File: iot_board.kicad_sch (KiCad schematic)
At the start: 4 parts, among them J1 SS-52400-003, J2 B2B-PH-SM4-TB, U2 MCP73871-2CAI_ML

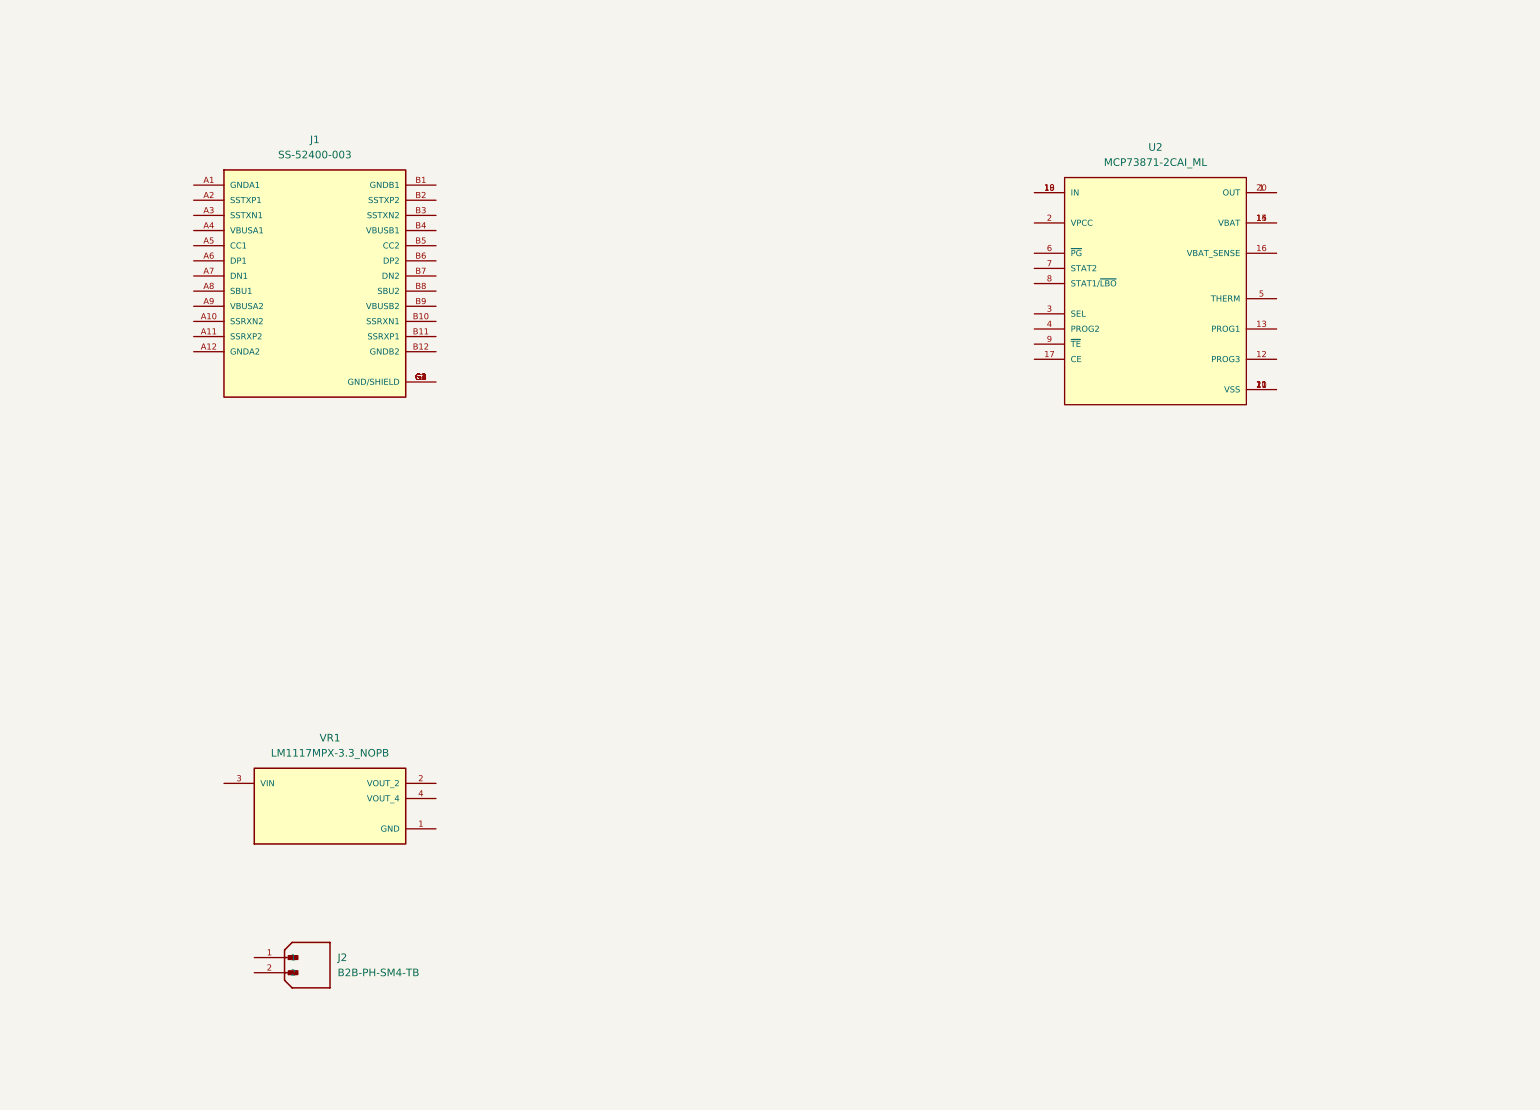
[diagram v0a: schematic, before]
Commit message: Connected the USB-C connector and the Li-Polymer battery charger
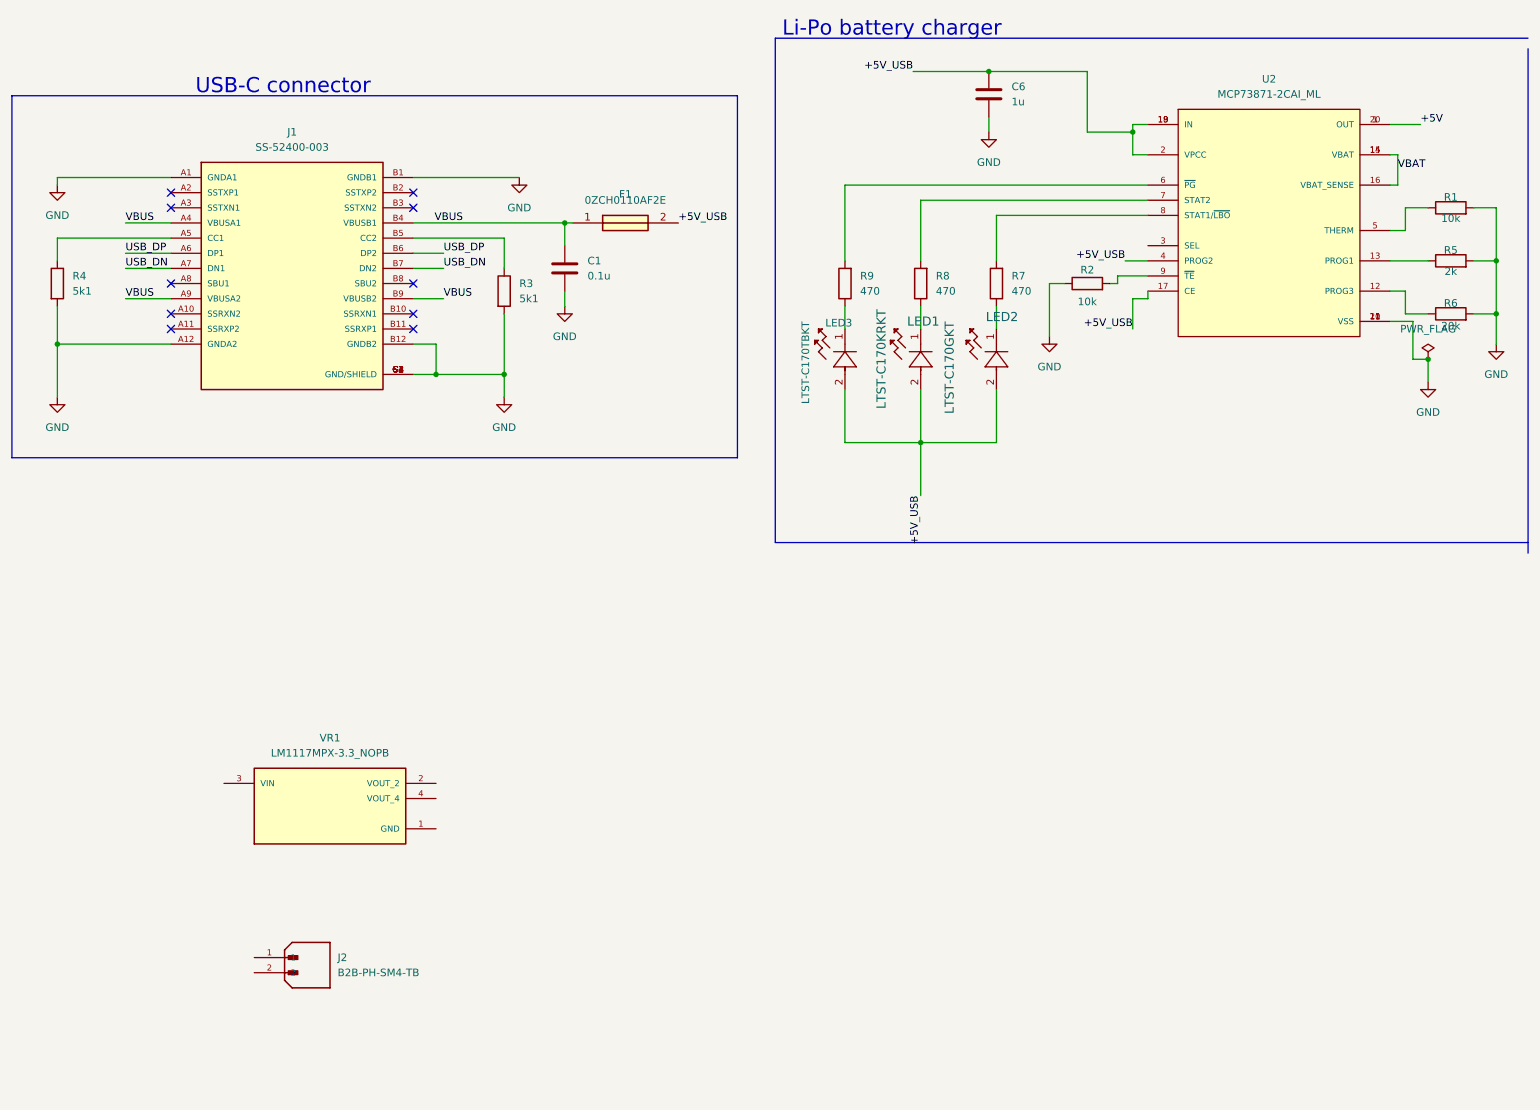
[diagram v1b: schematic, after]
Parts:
- added C1: 0.1u, symbol Device:C
- added C6: 1u, symbol Device:C
- added F1: 0ZCH0110AF2E, symbol ESP32_IoT_Board_Schem:0ZCH0110AF2E
- added LED1: LTST-C170KRKT, ESP32_IoT_Board_Footprint:LTST-C170KRKT, symbol ESP32_IoT_Board_Schem:LTST-C170KRKT
- added LED2: LTST-C170GKT, symbol ESP32_IoT_Board_Schem:LTST-C170GKT
- added LED3: LTST-C170TBKT, ESP32_IoT_Board_Footprint:LTST-C170TBKT, symbol ESP32_IoT_Board_Schem:LTST-C170TBKT
- added R1, R2: 10k, symbol Device:R
- added R3, R4: 5k1, symbol Device:R
- added R5: 2k, symbol Device:R
- added R6: 20k, symbol Device:R
- added R7, R8, R9: 470, symbol Device:R
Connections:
- net +5V: now reaches U2.1 (OUT), U2.20 (OUT)
- net GND: now reaches U2.10 (VSS), U2.11 (VSS), U2.21 (VSS)
- net GND: now also J1.A1 (GNDA1), J1.A12 (GNDA2), J1.B1 (GNDB1), J1.B12 (GNDB2), J1.G1 (GND/SHIELD), J1.G2 (GND/SHIELD), J1.G3 (GND/SHIELD), J1.G4 (GND/SHIELD), J1.S1 (GND/SHIELD), J1.S2 (GND/SHIELD), J1.S3 (GND/SHIELD), J1.S4 (GND/SHIELD), C1.2, C6.2, R1.2, R2.1, R3.2, R4.2, R5.2, R6.2
- net at U2.12 (PROG3): now also R6.1
- net at U2.13 (PROG1): now also R5.1
- net VBAT: now reaches U2.14 (VBAT), U2.15 (VBAT)
- net VBAT: now also U2.16 (VBAT_SENSE)
- net +5V_USB: now reaches U2.17 (CE)
- net +5V_USB: now also U2.18 (IN), U2.19 (IN), U2.2 (VPCC), U2.4 (PROG2), C6.1, F1.2, LED1.2, LED2.2, LED3.2
- net at U2.5 (THERM): now also R1.1
- net at U2.6 (~{PG}): now also R9.2
- net at U2.7 (STAT2): now also R8.2
- net at U2.8 (STAT1/~{LBO}): now also R7.2
- net at U2.9 (~{TE}): now also R2.2
- net VBUS: now reaches J1.A4 (VBUSA1)
- net VBUS: now also J1.A9 (VBUSA2), J1.B4 (VBUSB1), J1.B9 (VBUSB2), C1.1, F1.1
- net at J1.A5 (CC1): now also R4.1
- net USB_DP: now reaches J1.A6 (DP1)
- net USB_DP: now also J1.B6 (DP2)
- net USB_DN: now reaches J1.A7 (DN1)
- net USB_DN: now also J1.B7 (DN2)
- net at J1.B5 (CC2): now also R3.1
- new net: LED1.1, R8.1
- new net: LED3.1, R9.1
- new net: LED2.1, R7.1
- no-connect marks 0 -> 10
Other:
- note added: "Li-Po battery charger"
- note added: "USB-C connector"
- moved on the sheet: J1, U2

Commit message: Added ESP32 microcontroller and SMD card connector
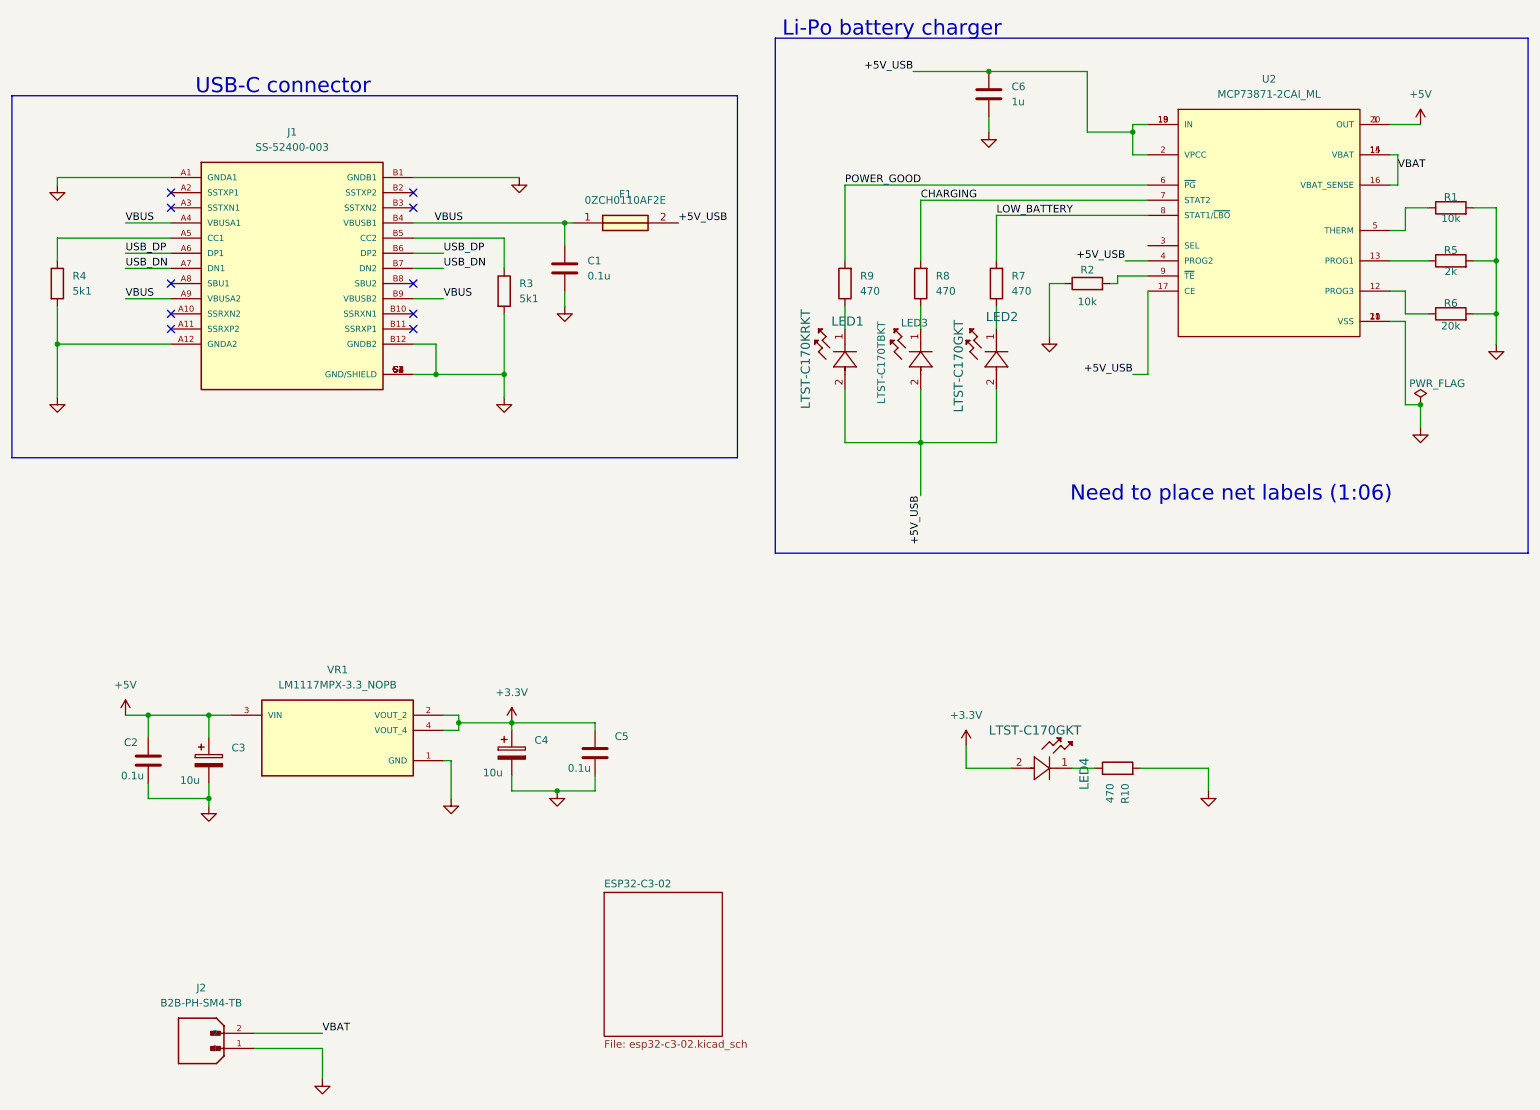
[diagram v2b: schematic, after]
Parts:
- added C2, C5: 0.1u, symbol Device:C
- added C3, C4: 10u, symbol Device:C_Polarized
- added LED4: LTST-C170GKT, symbol ESP32_IoT_Board_Schem:LTST-C170GKT
- added R10: 470, symbol Device:R
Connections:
- net +5V: now also VR1.3 (VIN), C2.1, C3.1
- net GND: now also J2.1, VR1.1 (GND), C2.2, C3.2, C4.2, C5.2, R10.2
- net VBAT: now also J2.2
- net +3.3V: now reaches VR1.2 (VOUT_2)
- net +3.3V: now also VR1.4 (VOUT_4), C4.1, C5.1, LED4.2
- net at R8.1: now also LED3.1; no longer LED1.1
- net CHARGING: now reaches R8.2, U2.7 (STAT2)
- net at R9.1: now also LED1.1; no longer LED3.1
- net POWER_GOOD: now reaches R9.2, U2.6 (~{PG})
- net LOW_BATTERY: now reaches R7.2, U2.8 (STAT1/~{LBO})
- new net: LED4.1, R10.1
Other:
- added sheet ESP32-C3-02 (esp32-c3-02.kicad_sch)
- note added: "Need to place net labels (1:06)"
- moved on the sheet: J2, LED1, LED3, VR1

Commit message: Connected USB to UART connector, ESP32 controller and the SD card module
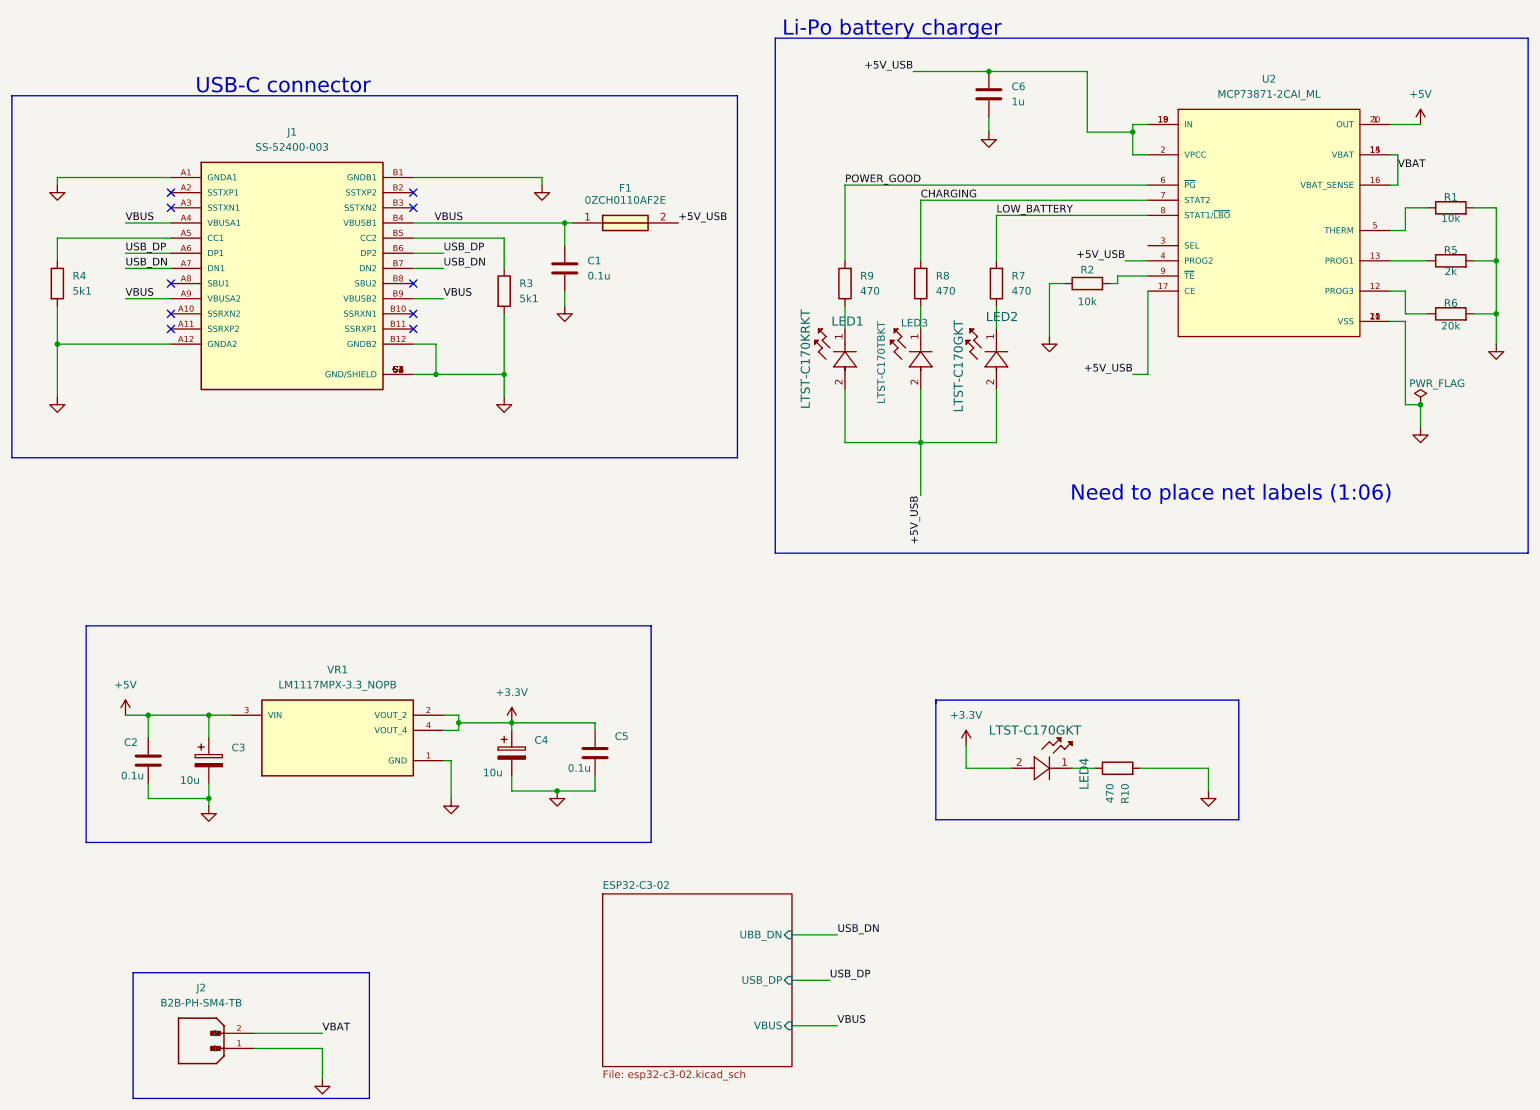
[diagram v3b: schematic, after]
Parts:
- F1: footprint (none) -> ESP32_IoT_Board_Footprint:0ZCH0110AF2E
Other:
- sheet ESP32-C3-02 ports: added UBB_DN, USB_DP, VBUS; removed none
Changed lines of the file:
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@@
 	(wire
 		(pts
+			(xy 146.05 166.37) (xy 153.67 166.37)
+		)
+		(stroke
+			(width 0)
+			(type default)
+		)
+	)
+	(wire
+		(pts
 			(xy 34.29 129.54) (xy 38.1 129.54)
 		)
@@
 		)
 	)
+	(polyline
+		(pts
+			(xy 170.18 147.066) (xy 220.98 147.066)
+		)
+		(stroke
+			(width 0)
+			(type default)
+		)
+	)
 	(wire
 		(pts
@@
 		)
 	)
+	(polyline
+		(pts
+			(xy 122.428 150.876) (xy 122.428 114.554)
+		)
+		(stroke
+			(width 0)
+			(type default)
+		)
+	)
 	(wire
 		(pts
@@
 	(polyline
 		(pts
+			(xy 27.686 114.554) (xy 122.428 114.554)
+		)
+		(stroke
+			(width 0)
+			(type default)
+		)
+	)
+	(polyline
+		(pts
+			(xy 35.56 172.72) (xy 75.184 172.72)
+		)
+		(stroke
+			(width 0)
+			(type default)
+		)
+	)
+	(polyline
+		(pts
 			(xy 136.906 25.654) (xy 136.906 86.36)
 		)
@@
 		)
 	)
+	(polyline
+		(pts
+			(xy 75.184 193.802) (xy 75.184 172.72)
+		)
+		(stroke
+			(width 0)
+			(type default)
+		)
+	)
+	(polyline
+		(pts
+			(xy 35.56 172.72) (xy 35.56 193.802)
+		)
+		(stroke
+			(width 0)
+			(type default)
+		)
+	)
+	(polyline
+		(pts
+			(xy 27.686 150.876) (xy 122.428 150.876)
+		)
+		(stroke
+			(width 0)
+			(type default)
+		)
+	)
 	(wire
 		(pts
@@
 		)
 	)
+	(polyline
+		(pts
+			(xy 170.18 127) (xy 170.18 127.508)
+		)
+		(stroke
+			(width 0)
+			(type default)
+		)
+	)
 	(wire
 		(pts
@@
 		)
 	)
+	(polyline
+		(pts
+			(xy 27.686 114.554) (xy 27.686 150.876)
+		)
+		(stroke
+			(width 0)
+			(type default)
+		)
+	)
 	(wire
 		(pts
@@
 		)
 	)
+	(polyline
+		(pts
+			(xy 220.98 127) (xy 170.18 127)
+		)
+		(stroke
+			(width 0)
+			(type default)
+		)
+	)
 	(wire
 		(pts
@@
 	(wire
 		(pts
+			(xy 146.05 173.99) (xy 152.4 173.99)
+		)
+		(stroke
+			(width 0)
+			(type default)
+		)
+	)
+	(wire
+		(pts
 			(xy 34.29 52.07) (xy 41.91 52.07)
 		)
@@
 		)
 	)
+	(polyline
+		(pts
+			(xy 220.98 147.066) (xy 220.98 127)
+		)
+		(stroke
+			(width 0)
+			(type default)
+		)
+	)
 	(wire
 		(pts
@@
 	(wire
 		(pts
-			(xy 246.38 58.42) (xy 248.92 58.42)
+			(xy 104.14 40.64) (xy 104.14 39.37)
 		)
 		(stroke
@@
 	(wire
 		(pts
-			(xy 82.55 39.37) (xy 100.33 39.37)
+			(xy 104.14 39.37) (xy 82.55 39.37)
+		)
+		(stroke
+			(width 0)
+			(type default)
+		)
+	)
+	(wire
+		(pts
+			(xy 246.38 58.42) (xy 248.92 58.42)
 		)
 		(stroke
@@
 		)
 	)
+	(polyline
+		(pts
+			(xy 35.56 193.802) (xy 75.184 193.802)
+		)
+		(stroke
+			(width 0)
+			(type default)
+		)
+	)
 	(wire
 		(pts
@@
 		)
 	)
+	(polyline
+		(pts
+			(xy 170.18 127) (xy 170.18 147.066)
+		)
+		(stroke
+			(width 0)
+			(type default)
+		)
+	)
 	(wire
 		(pts
@@
 		)
 	)
+	(wire
+		(pts
+			(xy 146.05 181.61) (xy 153.67 181.61)
+		)
+		(stroke
+			(width 0)
+			(type default)
+		)
+	)
 	(label "CHARGING"
 		(at 167.64 43.18 0)
@@
 		)
 	)
+	(label "USB_DN"
+		(at 153.67 166.37 0)
+		(effects
+			(font
+				(size 1.27 1.27)
+			)
+			(justify left bottom)
+		)
+	)
+	(label "VBUS"
+		(at 153.67 181.61 0)
+		(effects
+			(font
+				(size 1.27 1.27)
+			)
+			(justify left bottom)
+		)
+	)
+	(label "USB_DP"
+		(at 152.4 173.99 0)
+		(effects
+			(font
+				(size 1.27 1.27)
+			)
+			(justify left bottom)
+		)
+	)
 	(symbol
 		(lib_id "power:+3.3V")
@@
 		(dnp no)
 		(property "Reference" "F1"
-			(at 118.11 42.164 0)
+			(at 118.11 41.148 0)
 			(effects
 				(font
@@
 			)
 		)
-		(property "Footprint" ""
+		(property "Footprint" "ESP32_IoT_Board_Footprint:0ZCH0110AF2E"
 			(at 132.08 143.18 0)
 			(effects
@@
 	(symbol
 		(lib_id "power:GND")
-		(at 100.33 39.37 0)
+		(at 104.14 40.64 0)
 		(unit 1)
 		(exclude_from_sim no)
@@
 		(dnp no)
 		(property "Reference" "#PWR06"
-			(at 100.33 45.72 0)
+			(at 104.14 46.99 0)
 			(effects
 				(font
@@
 		)
 		(property "Value" "GND"
-			(at 100.33 44.45 0)
+			(at 104.14 45.72 0)
 			(effects
 				(font
@@
 		)
 		(property "Footprint" ""
-			(at 100.33 39.37 0)
+			(at 104.14 40.64 0)
 			(effects
 				(font
@@
 		)
 		(property "Datasheet" ""
-			(at 100.33 39.37 0)
+			(at 104.14 40.64 0)
 			(effects
 				(font
@@
 		)
 		(property "Description" "Power symbol creates a global label with name \"GND\" , ground"
-			(at 100.33 39.37 0)
+			(at 104.14 40.64 0)
 			(effects
 				(font
@@
 	)
 	(sheet
-		(at 114.554 159.258)
-		(size 19.812 24.13)
+		(at 114.3 159.512)
+		(size 31.75 28.956)
 		(exclude_from_sim no)
 		(in_bom yes)
@@
 		)
 		(property "Sheetname" "ESP32-C3-02"
-			(at 114.554 158.5464 0)
+			(at 114.3 158.8004 0)
 			(effects
 				(font
@@
 		)
 		(property "Sheetfile" "esp32-c3-02.kicad_sch"
-			(at 114.554 183.9726 0)
+			(at 114.3 189.0526 0)
 			(effects
 				(font
@@
 			)
 		)
+		(pin "UBB_DN" input
+			(at 146.05 166.37 0)
+			(effects
+				(font
+					(size 1.27 1.27)
+				)
+				(justify right)
+			)
+		)
+		(pin "USB_DP" input
+			(at 146.05 173.99 0)
+			(effects
+				(font
+					(size 1.27 1.27)
+				)
+				(justify right)
+			)
+		)
+		(pin "VBUS" input
+			(at 146.05 181.61 0)
+			(effects
+				(font
+					(size 1.27 1.27)
+				)
+				(justify right)
+			)
+		)
